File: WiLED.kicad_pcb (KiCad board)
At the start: 2 copper layers, 37 x 83 mm, 57 parts, among them P1 Serial to USB, P2 DC In, P3 Lamp Connector, P4 LED Out, SW1 Reset, SW2 Boot, SW3 Toggle, SW4 Rotary Encoder, U1 ESP-WROOM-32, U2 VXO7803-500, U3 AL8860WT-7, U4 HC-SR501

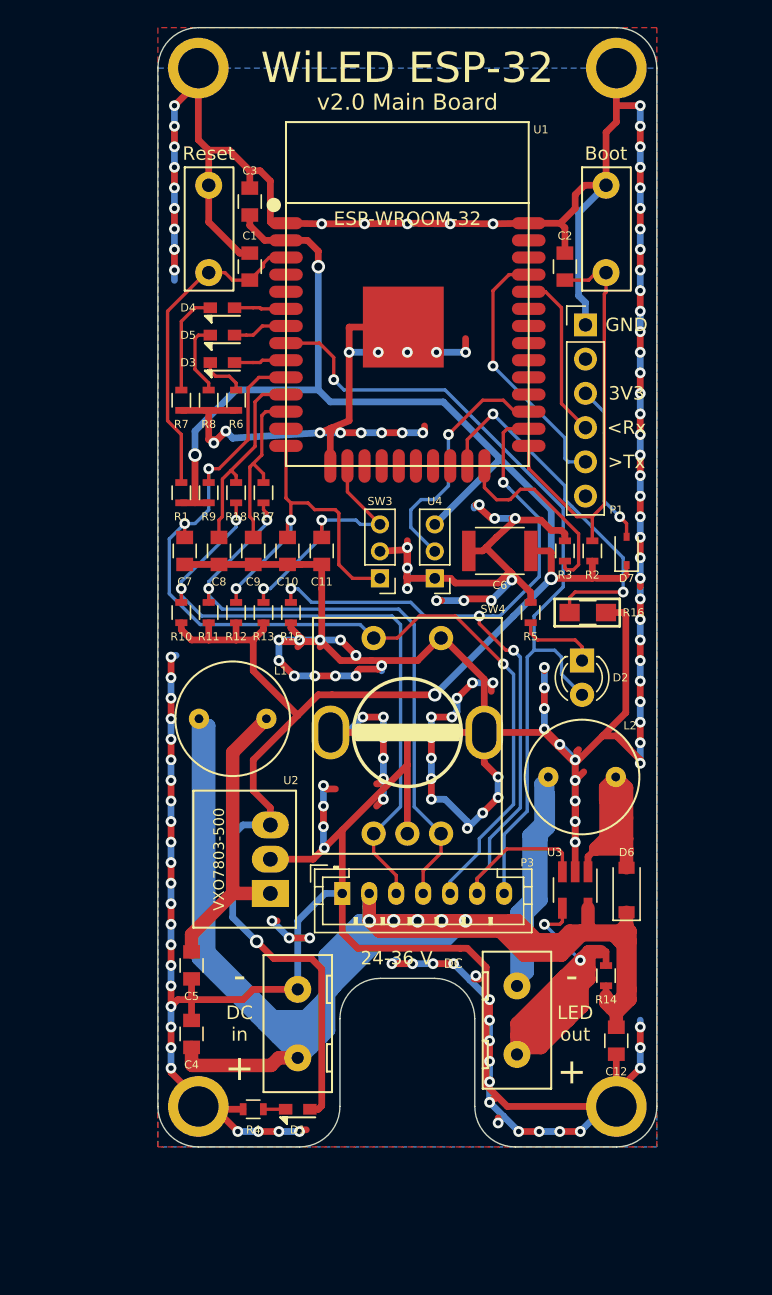
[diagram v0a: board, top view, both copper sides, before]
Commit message: Update PCB for KiCad 5, and begin rerouting for new PSU
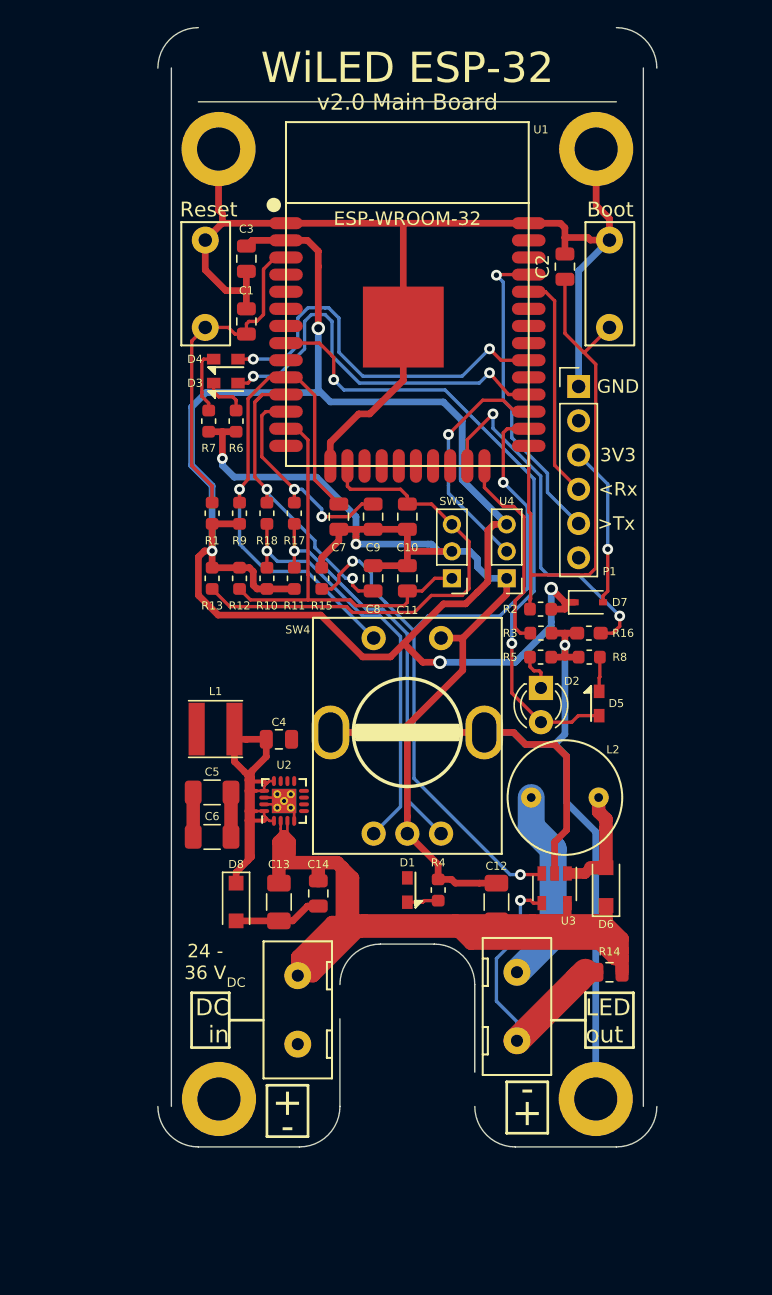
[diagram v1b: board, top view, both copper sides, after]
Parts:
- removed P3: Lamp Connector, Connectors_JST:JST_PH_B7B-PH-K_07x2.00mm_Straight
- removed REF** (x4): M2.5_hole, custom-footprints:M3_hole
- removed REF***: OSHW-Logo_19x20mm_SilkScreen, Symbols:OSHW-Logo_19x20mm_SilkScreen
- removed REF***: WEEE-Logo_5.6x8mm_SilkScreen, Symbols:WEEE-Logo_5.6x8mm_SilkScreen
- added C13: 10uF, Capacitor_SMD:C_1206_3216Metric, F.Cu at (163.2, 116.2)
- added C14: 100nF, Capacitor_SMD:C_0805_2012Metric, F.Cu at (166.1, 115.6)
- added D8: SS14FL, Diode_SMD:D_SOD-123F, F.Cu at (160.0, 116.2)
- added J1: Mount, MountingHole:MountingHole_3.2mm_M3_ISO14580_Pad, F.Cu at (158.7, 60.4)
- added J2: Mount, MountingHole:MountingHole_3.2mm_M3_ISO14580_Pad, F.Cu at (186.7, 60.4)
- added J3: Mount, MountingHole:MountingHole_3.2mm_M3_ISO14580_Pad, F.Cu at (158.8, 130.8)
- added J4: Mount, MountingHole:MountingHole_3.2mm_M3_ISO14580_Pad, F.Cu at (186.7, 130.8)
- C1, C10, C11, C2, C3, C7, C8, C9: footprint Capacitors_SMD:C_0805 -> Capacitor_SMD:C_0805_2012Metric
- C12: footprint Capacitors_SMD:C_0805 -> Capacitor_SMD:C_1206_3216Metric
- C4: value 4.7uF -> 22nF; footprint Capacitors_SMD:C_0805 -> Capacitor_SMD:C_0805_2012Metric
- C5: value 10uF -> 22uF; footprint Capacitors_SMD:C_0805 -> Capacitor_SMD:C_1206_3216Metric
- C6: value 100uF -> 22uF; footprint Capacitors_SMD:C_1812 -> Capacitor_SMD:C_1206_3216Metric
- D2: value Indicator LED -> Ind. LED 1
- D5: value Status 3 LED -> Ind. LED 2
- D6: footprint Diodes_SMD:D_SOD-123 -> Diode_SMD:D_SOD-123F
- D7: footprint Diodes_SMD:D_SOD-323 -> Diode_SMD:D_SOD-323
- L1: value 12 uH -> 4.7uH; footprint custom-footprints:THT_Inductor_5mm -> Inductor_SMD:L_Taiyo-Yuden_NR-40xx
- R1, R10, R11, R12, R13, R15, R17, R18, R2, R3, R9: footprint Resistors_SMD:R_0603 -> Resistor_SMD:R_0603_1608Metric
- R14: footprint Resistors_SMD:R_0603 -> Resistor_SMD:R_0805_2012Metric
- R16: footprint Resistors_SMD:R_0805_HandSoldering -> Resistor_SMD:R_0603_1608Metric_Pad1.05x0.95mm_HandSolder
- R4, R5, R7: value 680 -> 330; footprint Resistors_SMD:R_0603 -> Resistor_SMD:R_0603_1608Metric
- R6, R8: value 680 -> 1k; footprint Resistors_SMD:R_0603 -> Resistor_SMD:R_0603_1608Metric
- U2: value VXO7803-500 -> TS3004x; footprint custom-footprints:VXO78-500 -> Package_DFN_QFN:QFN-16-1EP_3x3mm_P0.5mm_EP2.7x2.7mm_ThermalVias
- U3: footprint TO_SOT_Packages_SMD:SOT-23-5_HandSoldering -> Package_TO_SOT_SMD:SOT-23-5
- moved D5 39.1 mm to (186.9, 101.5), turned to 270 degrees
- moved R8 34.0 mm to (186.2, 98.0), turned to 0 degrees
- moved C6 30.1 mm to (158.2, 111.4), turned to 0 degrees
- moved C4 22.8 mm to (163.2, 104.1), turned to 180 degrees
- moved R4 21.3 mm to (175.0, 115.3), turned to 270 degrees
- moved D1 18.2 mm to (172.7, 115.3), turned to 90 degrees
- moved C12 13.6 mm to (179.3, 116.2), turned to 90 degrees
- moved C5 12.9 mm to (158.2, 108.1), turned to 0 degrees
- moved C7 11.7 mm to (167.6, 87.6)
- moved C8 11.6 mm to (170.2, 92.2), turned to 90 degrees
- moved C9 9.25 mm to (170.2, 87.6)
- moved C10 9.12 mm to (172.7, 92.2), turned to 90 degrees
- moved R10 6.84 mm to (162.3, 92.2)
- moved C11 6.84 mm to (172.7, 87.6)
- moved R11 6.84 mm to (164.3, 92.2)
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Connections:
- C4 pad 1: RAW -> Net-(C4-Pad1)
- C4 pad 2: GND -> Net-(C4-Pad2)
- C5 pad 1: Net-(C5-Pad1) -> +3V3
- D3 pad 2: IO33 -> IO17
- D4 pad 2: IO34 -> IO18
- D5 pad 2: IO35 -> IND_PWM
- L1 pad 1: RAW -> Net-(C4-Pad2)
- L1 pad 2: Net-(C5-Pad1) -> +3V3
- P1 pad 2: Net-(P1-Pad2) -> (no net)
- P1 pad 6: Net-(P1-Pad6) -> (no net)
- P2 pad 1: GND -> RAW
- P2 pad 2: RAW -> GND
- SW4 pad : GND -> (no net)
- U1 pad 13: Net-(U1-Pad13) -> TGL_1
- U1 pad 14: TGL_1 -> (no net)
- U1 pad 17: Net-(U1-Pad17) -> (no net)
- U1 pad 18: Net-(U1-Pad18) -> (no net)
- U1 pad 19: Net-(U1-Pad19) -> (no net)
- U1 pad 20: Net-(U1-Pad20) -> (no net)
- U1 pad 21: Net-(U1-Pad21) -> (no net)
- U1 pad 22: Net-(U1-Pad22) -> (no net)
- U1 pad 28: Net-(U1-Pad28) -> IO17
- U1 pad 29: Net-(U1-Pad29) -> (no net)
- U1 pad 30: Net-(U1-Pad30) -> IO18
- U1 pad 31: Net-(U1-Pad31) -> (no net)
- U1 pad 32: Net-(U1-Pad32) -> (no net)
- U1 pad 33: Net-(U1-Pad33) -> (no net)
- U1 pad 36: Net-(U1-Pad36) -> (no net)
- U1 pad 37: Net-(U1-Pad37) -> (no net)
- U1 pad 4: Net-(U1-Pad4) -> (no net)
- U1 pad 5: Net-(U1-Pad5) -> (no net)
- U1 pad 6: IO34 -> (no net)
- U1 pad 7: IO35 -> (no net)
- U1 pad 9: IO33 -> (no net)
- U2 pad 1: Net-(C5-Pad1) -> Net-(C4-Pad2)
- U2 pad 2: GND -> RAW
- U2 pad 3: +3V3 -> RAW
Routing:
- net GND: track 587.8 -> 257.1 mm, vias 161 -> 3
- net RAW: track 220.8 -> 103.6 mm, vias 5 -> 0
- net Net-(C4-Pad2): track 0.00 -> 33.3 mm
- net ENC_SW: track 71.3 -> 40.0 mm, vias 3 -> 1
- net IO17: track 0.00 -> 30.2 mm, vias 0 -> 2
- net IO18: track 0.00 -> 29.9 mm, vias 0 -> 2
- net +3V3: track 157.7 -> 128.3 mm, vias 5 -> 4
- net LED_POS: track 49.7 -> 21.5 mm, vias 2 -> 1
- net Net-(C5-Pad1): track 22.4 -> 0.00 mm
- net LED_NEG: track 32.2 -> 14.7 mm
- net CON_B: track 47.5 -> 30.2 mm, vias 2 -> 1
- net TGL_2: track 19.3 -> 36.6 mm, vias 2 -> 0
- net CON_A: track 48.3 -> 31.2 mm, vias 2 -> 1
- net Net-(D6-Pad2): track 25.3 -> 8.34 mm
- net IND_PWM: track 62.7 -> 47.7 mm, vias 1 -> 2
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- removed copper zone on B.Cu, net GND
- removed copper zone on F.Cu, net GND
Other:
- outline, holes or cut-outs redrawn
- net class 3V3: clearance 0.25 -> 0.2; trace_width 0.5 -> 0.2
- net class Default: clearance 0.25 -> 0.2; trace_width 0.25 -> 0.2
- net class POWER: clearance 0.25 -> 0.2
- rule trace_clearance: 0.25 -> 0.2
- rule trace_min: 0.25 -> 0.2
- board text added: "24 - 36 V"
- board text removed: "24-36 V"

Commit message: Initial complete routing of PCB for v2.1
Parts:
- added REF**: L_Taiyo-Yuden_NR-60xx, Inductor_SMD:L_Taiyo-Yuden_NR-60xx, F.Cu at (184.4, 108.5)
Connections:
- SW4 pad : (no net) -> GND
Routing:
- net GND: track 257.1 -> 308.6 mm
- net +3V3: track 128.3 -> 167.1 mm, vias 4 -> 6
- net RAW: track 103.6 -> 87.4 mm, vias 0 -> 14
- net Net-(C4-Pad1): track 0.00 -> 3.22 mm
- net Net-(D6-Pad2): track 8.34 -> 11.2 mm
- net LED_PWM: track 58.4 -> 59.2 mm
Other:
- board size 37 x 83 mm -> 35 x 77.5 mm
- net class 3V3: clearance 0.2 -> 0.25; trace_width 0.2 -> 0.25
- net class Default: clearance 0.2 -> 0.25; trace_width 0.2 -> 0.25
- net class POWER: trace_width 1 -> 0.25
- rule trace_clearance: 0.2 -> 0.25

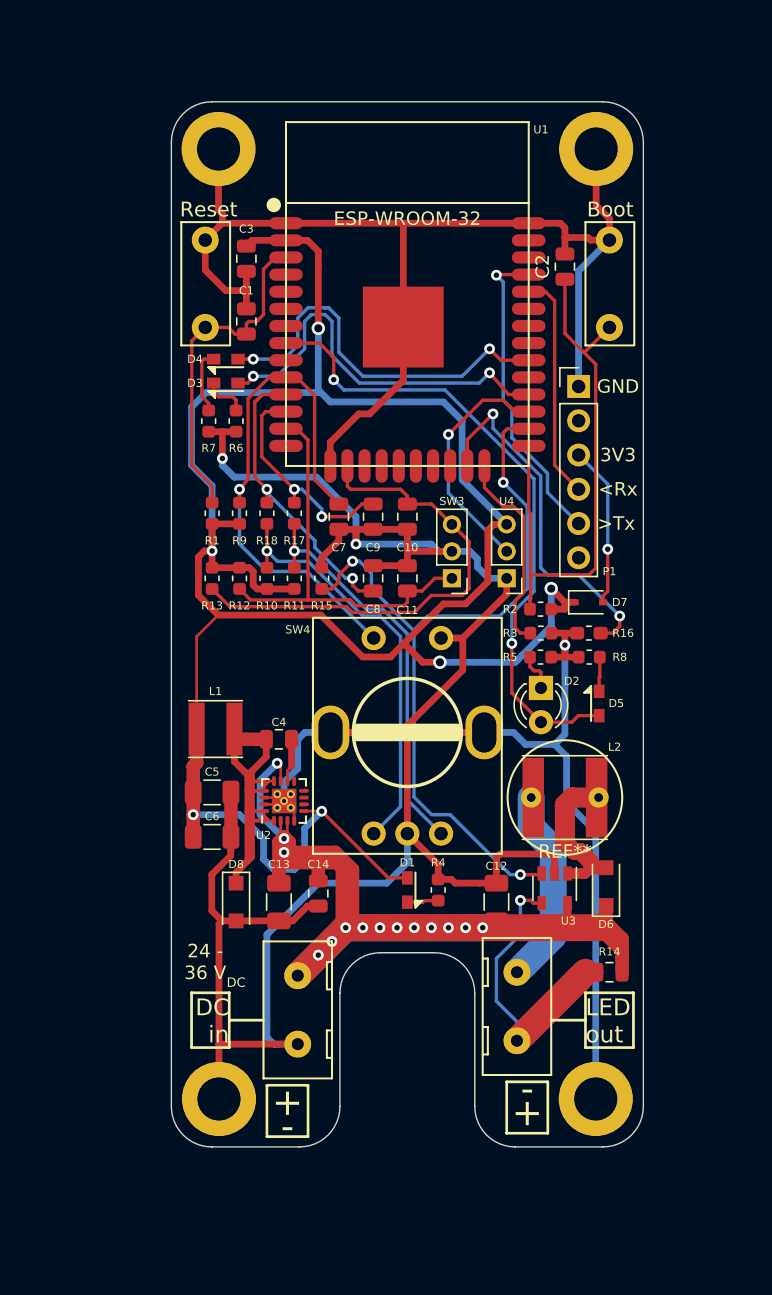
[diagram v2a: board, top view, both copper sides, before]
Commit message: Re-designed layout, with less wasted space
Routing is completed, but vias still need to be added. The newer layout
is much more space efficient.
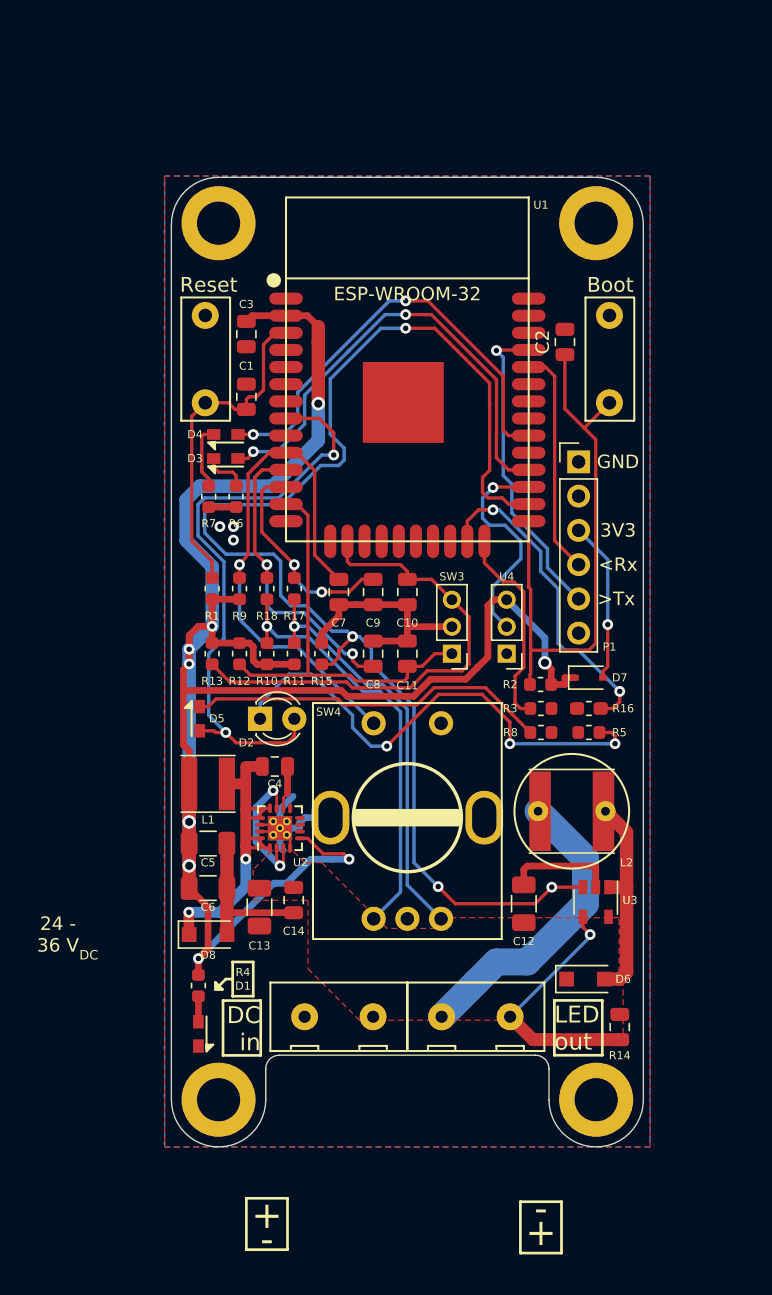
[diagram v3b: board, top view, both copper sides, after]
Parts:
- moved D5 29.6 mm to (157.3, 102.6)
- moved D2 21.0 mm to (161.8, 102.6), turned to 0 degrees
- moved R4 19.1 mm to (157.2, 122.4), turned to 90 degrees
- moved D1 18.8 mm to (157.2, 126.0)
- moved D6 7.03 mm to (185.9, 121.9), turned to 0 degrees
- moved R8 6.64 mm to (182.6, 103.6), turned to 180 degrees
- moved R5 6.64 mm to (186.2, 103.6), turned to 0 degrees
- moved SW4 6.32 mm to (172.7, 110.0)
- moved C10 5.59 mm to (172.7, 97.8)
- moved C11 5.59 mm to (172.7, 93.2)
- moved C2 5.59 mm to (184.4, 74.7)
- moved C3 5.59 mm to (160.8, 74.1)
- moved C7 5.59 mm to (167.6, 93.2)
- moved C8 5.59 mm to (170.2, 97.8)
- moved C9 5.59 mm to (170.2, 93.2)
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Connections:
- D1 pad 1: Net-(D1-Pad1) -> GND
- D1 pad 2: +3V3 -> Net-(D1-Pad2)
- R4 pad 1: GND -> Net-(D1-Pad2)
- R4 pad 2: Net-(D1-Pad1) -> +3V3
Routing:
- net GND: track 308.6 -> 52.6 mm
- net RAW: track 87.4 -> 10.8 mm, vias 14 -> 2
- net LED_PWM: track 59.2 -> 99.8 mm, vias 3 -> 4
- net Net-(D2-Pad1): track 2.85 -> 37.0 mm, vias 0 -> 3
- net Net-(D5-Pad1): track 2.56 -> 26.8 mm
- net +3V3: track 167.1 -> 153.7 mm, vias 6 -> 9
- net LED_NEG: track 14.7 -> 22.5 mm
- net Net-(C4-Pad2): track 33.3 -> 25.8 mm, vias 0 -> 2
- net IO17: track 30.2 -> 36.0 mm
- net IO18: track 29.9 -> 34.2 mm
- net Net-(D6-Pad2): track 11.2 -> 15.4 mm
- net Net-(R16-Pad1): track 27.3 -> 24.4 mm
- net LED_POS: track 21.5 -> 18.9 mm
- net IND_PWM: track 47.7 -> 45.1 mm
- net Net-(D1-Pad1): track 2.33 -> 0.00 mm
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- added copper zone on B.Cu, net GND
- added copper zone on F.Cu, net GND
- added copper zone on F.Cu, net RAW
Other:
- board size 35 x 77.5 mm -> 35 x 71.9 mm
- net class 3V3: trace_width 0.25 -> 0.5
- net class POWER: clearance 0.2 -> 0.25; trace_width 0.25 -> 0.5

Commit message: Add ground planes
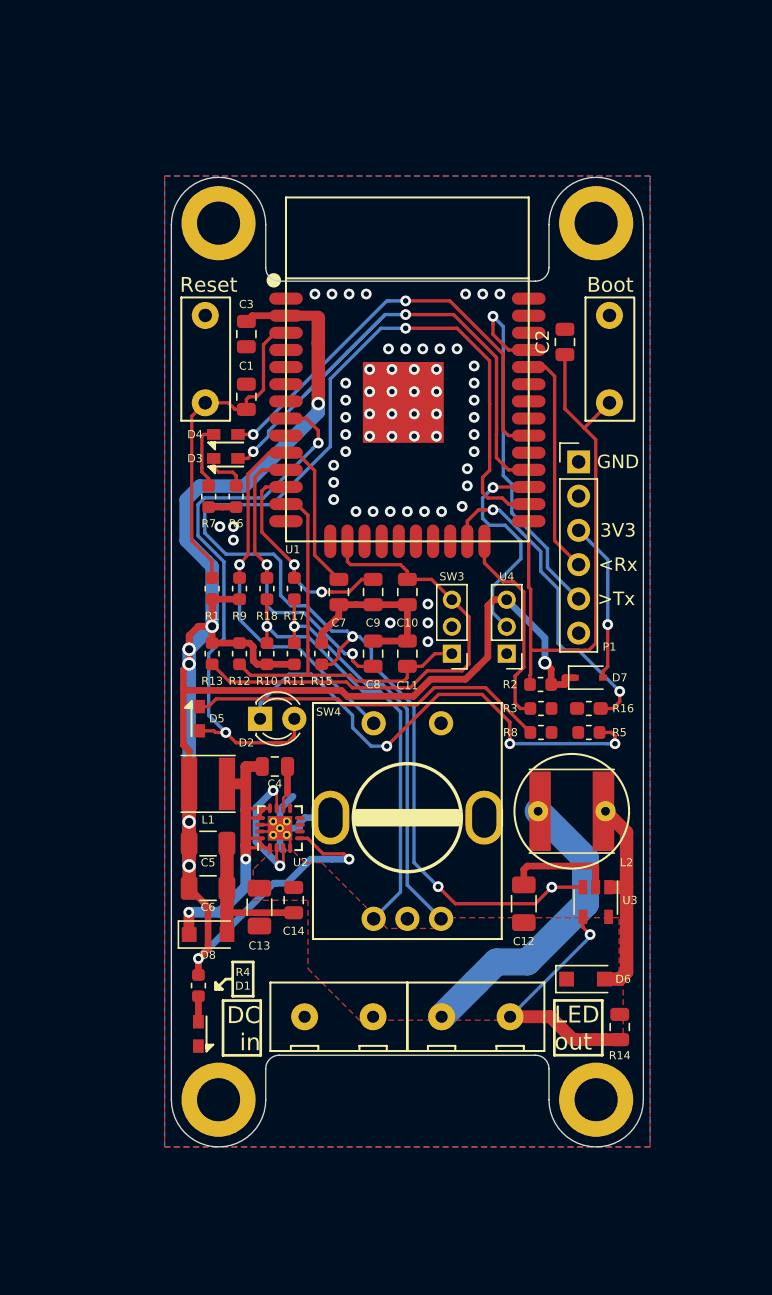
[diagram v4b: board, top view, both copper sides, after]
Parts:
- added REF**: OSHW-Logo2_14.6x12mm_SilkScreen, Symbol:OSHW-Logo2_14.6x12mm_SilkScreen, B.Cu at (172.7, 87.5)
- added REF**: WEEE-Logo_5.6x8mm_SilkScreen, Symbol:WEEE-Logo_5.6x8mm_SilkScreen, B.Cu at (172.7, 110.0)
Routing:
- net IO17: track 36.0 -> 44.3 mm
- net TX: track 23.4 -> 28.1 mm
- net GND: track 52.6 -> 49.3 mm, vias 3 -> 58
- net IND_PWM: track 45.1 -> 42.4 mm
- net +3V3: track 153.7 -> 152.2 mm
- net LED_PWM: track 99.8 -> 98.7 mm
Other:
- outline, holes or cut-outs redrawn
- board text added: "v2.2 Main Board"
- board text removed: "Fit R16 to disable boot debug messages"
- board text removed: "v2.0 Main Board"

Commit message: Add further stitching vias, layout mostly complete
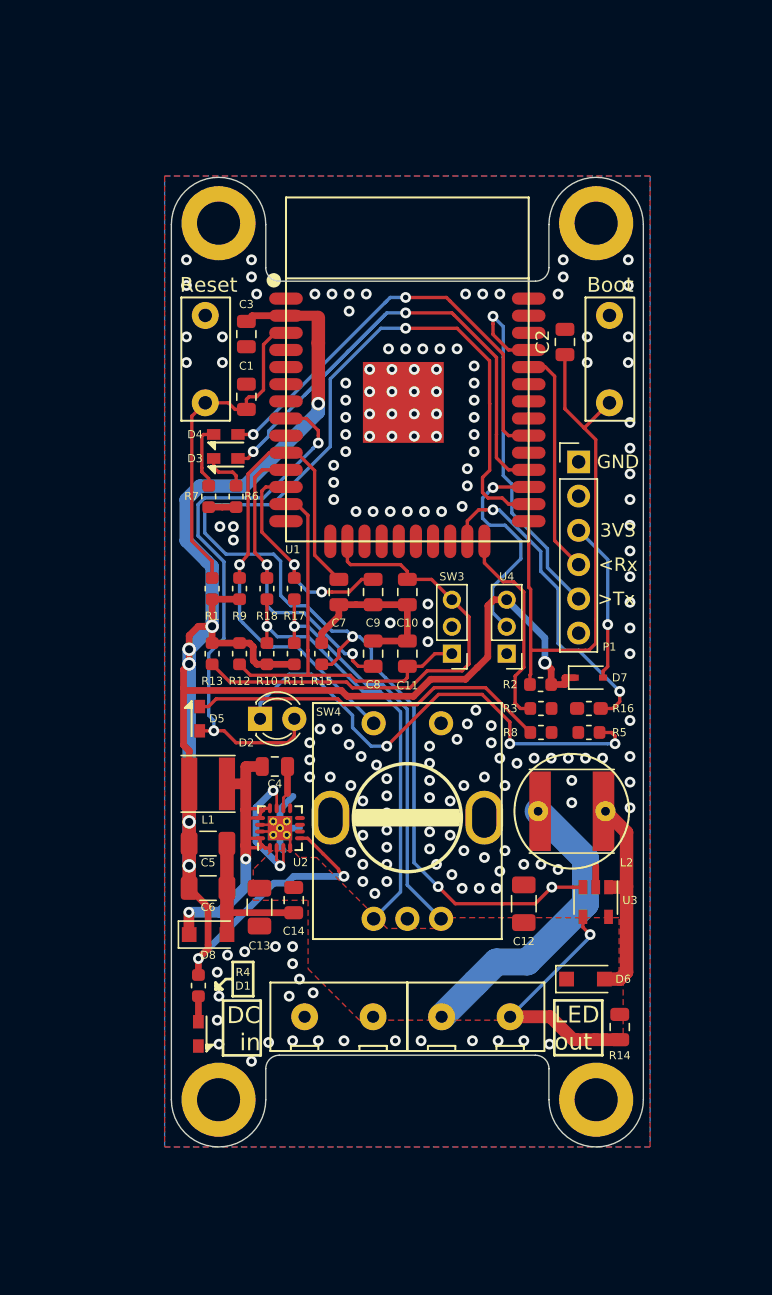
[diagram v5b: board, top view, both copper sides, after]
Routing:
- net GND: track 49.3 -> 40.0 mm, vias 58 -> 177
- net +3V3: track 152.2 -> 151.5 mm
- net IND_PWM: track 42.4 -> 41.7 mm
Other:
- rule via_min_size: 0.7 -> 0.8
- board text added: "v2.1 Main Board"
- board text removed: "v2.2 Main Board"
